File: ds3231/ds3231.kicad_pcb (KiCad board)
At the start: 4 copper layers, 6 parts, among them U1 DS3231M

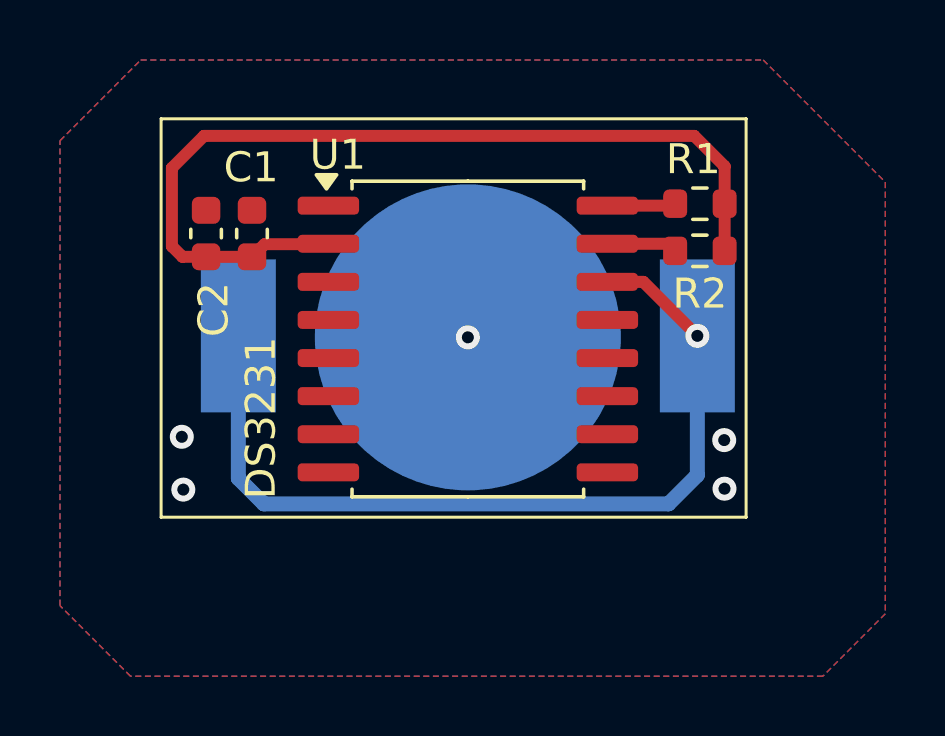
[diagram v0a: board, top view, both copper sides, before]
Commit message: [Rushil] corrected pcb added information on both schematic and pcb user drawing correct circuit of bno055
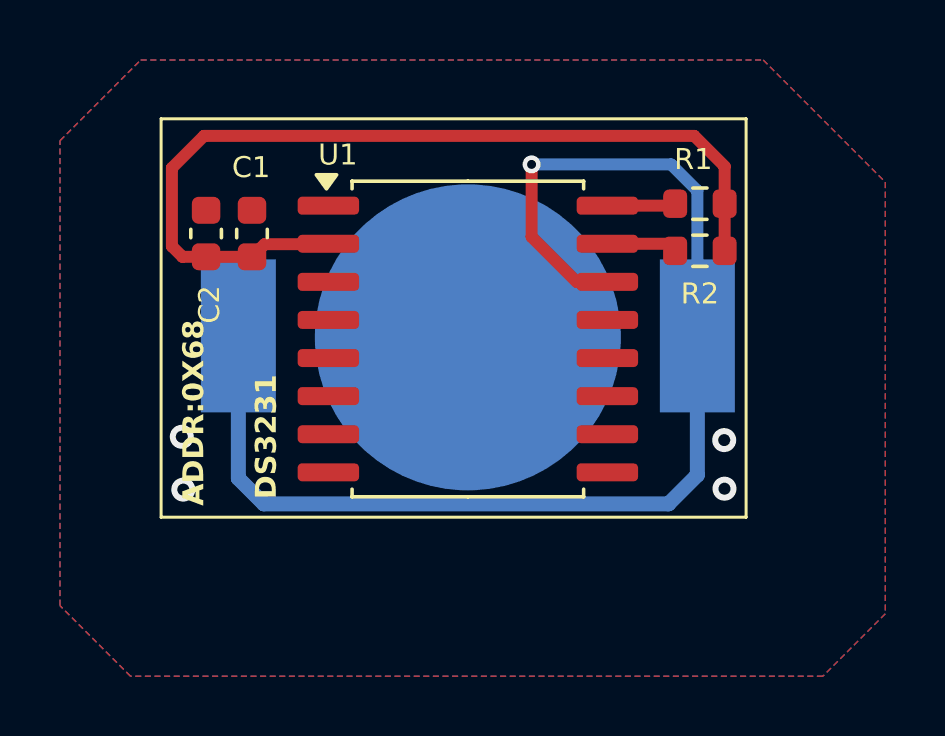
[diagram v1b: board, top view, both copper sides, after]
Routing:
- net Net-(U1-VBAT): track 29.2 -> 41.7 mm
- net /block_ds3231_rtc/GND: vias 5 -> 4
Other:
- board text added: "ADDR:0X68"
- board text added: "CR1216 / CR1225 BATTERY BACKUP ZONE(B COPPER LAYER) • 3V coin cell in surface mount holder • Backup power for DS3231 real-time clock • Do NOT use rechargeable cells • Avoid placing heat sources nearby • Ensure trace width to VBAT pin supports low standby current (~1 µA)"
- board text added: "DS3231M RTC Module(F COPPER LAYER) • Integrated MEMS oscillator - no crystal required • 32kHz + INT/SQW output optional • I2C @ 0x68 fixed address • VBAT powers RTC during VCC loss • Backup battery: CR1216/CR1225"
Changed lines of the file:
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@@
 			(effects
 				(font
-					(size 1 1)
-					(thickness 0.15)
+					(size 0.7 0.7)
+					(thickness 0.153)
 				)
 			)
@@
 			(effects
 				(font
-					(size 1 1)
-					(thickness 0.15)
+					(size 0.7 0.7)
+					(thickness 0.153)
 				)
 			)
@@
 		(tags "capacitor")
 		(property "Reference" "C2"
-			(at -2.535 0.25 90)
-			(layer "F.SilkS")
-			(effects
-				(font
-					(size 1 1)
-					(thickness 0.15)
+			(at -2.365 0.11 90)
+			(layer "F.SilkS")
+			(effects
+				(font
+					(size 0.7 0.7)
+					(thickness 0.153)
 				)
 			)
@@
 			(effects
 				(font
-					(size 1 1)
-					(thickness 0.15)
+					(size 0.7 0.7)
+					(thickness 0.153)
 				)
 			)
@@
 			(effects
 				(font
-					(size 1 1)
-					(thickness 0.15)
+					(size 0.7 0.7)
+					(thickness 0.153)
 				)
 			)
@@
 			(effects
 				(font
-					(size 1.4 1.4)
-					(thickness 0.15)
+					(size 0.7 0.7)
+					(thickness 0.153)
+					(bold yes)
 				)
 				(justify mirror)
@@
 		(effects
 			(font
-				(size 1 1)
-				(thickness 0.15)
+				(size 0.7 0.7)
+				(thickness 0.153)
+				(bold yes)
 			)
 			(justify left bottom)
 		)
 	)
+	(gr_text "ADDR:0X68"
+		(at 124.73 76.81 90)
+		(layer "F.SilkS")
+		(effects
+			(font
+				(size 0.7 0.7)
+				(thickness 0.153)
+				(bold yes)
+			)
+			(justify left bottom)
+		)
+	)
+	(gr_text "CR1216 / CR1225 BATTERY BACKUP ZONE(B COPPER LAYER)\n\n• 3V coin cell in surface mount holder  \n• Backup power for DS3231 real-time clock  \n• Do NOT use rechargeable cells  \n• Avoid placing heat sources nearby  \n• Ensure trace width to VBAT pin supports\n   low standby current (~1 µA)"
+		(at 123.48 70.36 0)
+		(layer "Dwgs.User")
+		(effects
+			(font
+				(size 0.4 0.4)
+				(thickness 0.1)
+				(bold yes)
+			)
+			(justify left bottom)
+		)
+	)
 	(gr_text "DS3231\n"
-		(at 127.15 76.62 90)
+		(at 124.06 76.48 0)
 		(layer "Dwgs.User")
 		(effects
@@
 		)
 	)
+	(gr_text " DS3231M RTC Module(F COPPER LAYER)\n• Integrated MEMS oscillator - no crystal required\n• 32kHz + INT/SQW output optional\n• I2C @ 0x68 fixed address\n• VBAT powers RTC during VCC loss\n• Backup battery: CR1216/CR1225\n"
+		(at 123.36 74.63 0)
+		(layer "Dwgs.User")
+		(effects
+			(font
+				(size 0.4 0.4)
+				(thickness 0.1)
+				(bold yes)
+			)
+			(justify left bottom)
+		)
+	)
 	(segment
-		(start 139.315 69.345)
-		(end 141.115 71.145)
+		(start 137.090001 69.345)
+		(end 135.59 67.844999)
 		(width 0.4)
 		(layer "F.Cu")
@@
 	)
 	(segment
-		(start 138.115 69.345)
-		(end 139.315 69.345)
+		(start 135.59 67.844999)
+		(end 135.59 65.43)
 		(width 0.4)
 		(layer "F.Cu")
 		(net 1)
 	)
+	(segment
+		(start 138.115 69.345)
+		(end 137.090001 69.345)
+		(width 0.4)
+		(layer "F.Cu")
+		(net 1)
+	)
 	(via
-		(at 141.115 71.145)
-		(size 0.8)
-		(drill 0.4)
+		(at 135.59 65.43)
+		(size 0.6)
+		(drill 0.3)
 		(layers "F.Cu" "B.Cu")
 		(net 1)
@@
 	)
 	(segment
+		(start 140.24 65.43)
+		(end 141.115 66.305)
+		(width 0.4)
+		(layer "B.Cu")
+		(net 1)
+	)
+	(segment
 		(start 126.666 76.746)
 		(end 140.154 76.746)
@@
 		(end 141.115 75.785)
 		(width 0.5)
+		(layer "B.Cu")
+		(net 1)
+	)
+	(segment
+		(start 135.59 65.43)
+		(end 140.24 65.43)
+		(width 0.4)
+		(layer "B.Cu")
+		(net 1)
+	)
+	(segment
+		(start 141.115 66.305)
+		(end 141.115 71.145)
+		(width 0.4)
 		(layer "B.Cu")
 		(net 1)
@@
 		(net 2)
 	)
-	(via
-		(at 133.465 71.195)
-		(size 0.8)
-		(drill 0.4)
-		(layers "F.Cu" "B.Cu")
-		(net 2)
-	)

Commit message: Edited and finalized blocks MCP9809 and DS3231
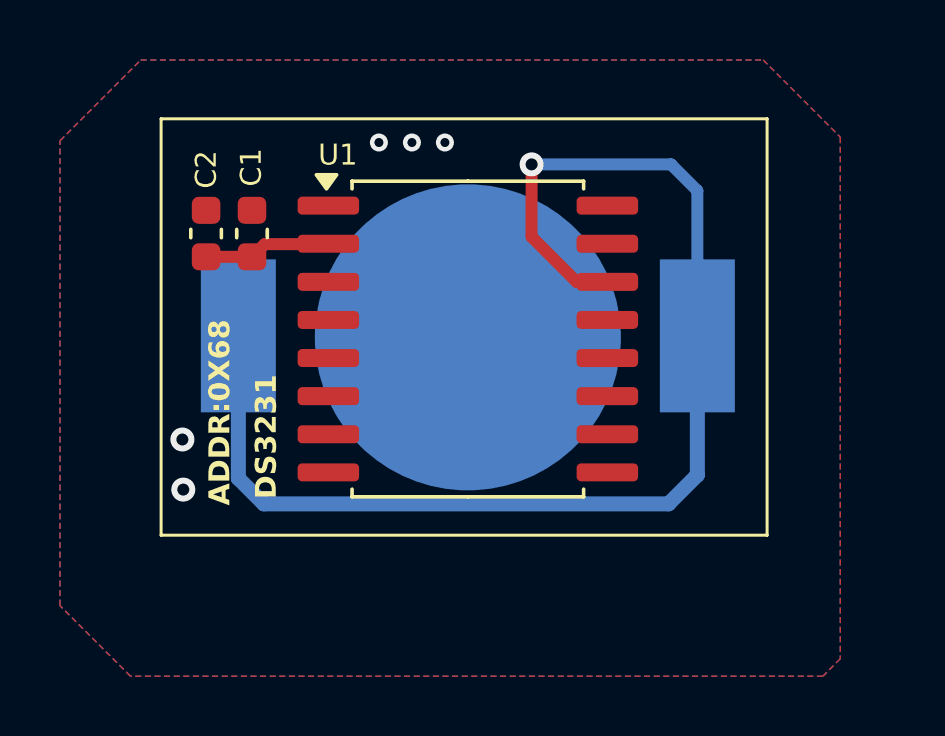
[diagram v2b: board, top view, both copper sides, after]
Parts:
- removed R1, R2: 10k, Library:R_0603_1608Metric
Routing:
- net /block_ds3231_rtc/VCC: track 30.3 -> 4.26 mm
- net Net-(U1-SDA): track 2.36 -> 0.00 mm
- net Net-(U1-SCL): track 2.29 -> 0.00 mm
- net /block_ds3231_rtc/GND: vias 4 -> 5
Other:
- board text added: "CR1216 / CR1225 BATTERY BACKUP ZONE • 3V coin cell in surface mount holder • Backup power for DS3231 real-time clock • Do NOT use rechargeable cells • Avoid placing heat sources nearby • Ensure trace width to VBAT pin supports low standby current (~1 µA)"
- board text removed: "CR1216 / CR1225 BATTERY BACKUP ZONE(B COPPER LAYER) • 3V coin cell in surface mount holder • Backup power for DS3231 real-time clock • Do NOT use rechargeable cells • Avoid placing heat sources nearby • Ensure trace width to VBAT pin supports low standby current (~1 µA)"
